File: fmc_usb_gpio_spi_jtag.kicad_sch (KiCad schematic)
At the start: 10 parts

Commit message: fmc_usb_gpio_spi_jtag.kicad_sch: update sheet pins
Signed-off-by: Huang Rui <vowstar@gmail.com>
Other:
- sheet FMC ports: added 12VP0, 3P3V, 3P3VAUX, GND, VADJ; removed none
- sheet GPIO ports: added GPIO[0..19]; removed none
- sheet JTAG ports: added JTAG{JTAG}; removed none
- sheet SDIO ports: added SDIO{SDIO}; removed none
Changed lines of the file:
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@@
       (effects (font (size 1.27 1.27)) (justify left top))
+    )
+    (pin "12VP0" output (at 260.35 50.8 270)
+      (effects (font (size 1.27 1.27)) (justify left))
+    )
+    (pin "3P3VAUX" output (at 257.81 50.8 270)
+      (effects (font (size 1.27 1.27)) (justify left))
+    )
+    (pin "GND" output (at 255.27 50.8 270)
+      (effects (font (size 1.27 1.27)) (justify left))
+    )
+    (pin "3P3V" output (at 252.73 50.8 270)
+      (effects (font (size 1.27 1.27)) (justify left))
+    )
+    (pin "VADJ" output (at 250.19 50.8 270)
+      (effects (font (size 1.27 1.27)) (justify left))
     )
     (instances
@@
       (effects (font (size 1.27 1.27)) (justify left top))
     )
-    (pin "USB_FS{USB_FS}" bidirectional (at 219.71 76.2 90)
+    (pin "USB_FS{USB_FS}" bidirectional (at 215.9 76.2 90)
       (effects (font (size 1.27 1.27)) (justify right))
     )
@@
       (effects (font (size 1.27 1.27)) (justify left top))
     )
+    (pin "JTAG{JTAG}" input (at 50.8 76.2 90)
+      (effects (font (size 1.27 1.27)) (justify right))
+    )
     (instances
       (project "fmc_usb_gpio_spi_jtag"
@@
     (property "Sheetfile" "gpio.kicad_sch" (at 137.16 107.2646 0)
       (effects (font (size 1.27 1.27)) (justify left top))
+    )
+    (pin "GPIO[0..19]" input (at 151.13 76.2 90)
+      (effects (font (size 1.27 1.27)) (justify right))
     )
     (instances
@@
       (effects (font (size 1.27 1.27)) (justify left top))
     )
+    (pin "SDIO{SDIO}" input (at 182.88 76.2 90)
+      (effects (font (size 1.27 1.27)) (justify right))
+    )
     (instances

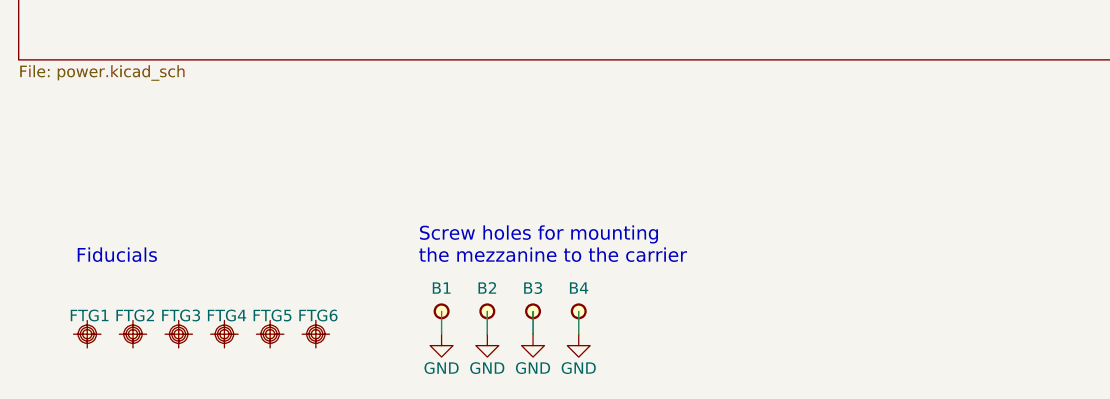
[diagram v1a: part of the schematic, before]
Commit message: fmc_usb_gpio_spi_jtag.kicad_sch: update fiducial and holes
Signed-off-by: Huang Rui <vowstar@gmail.com>
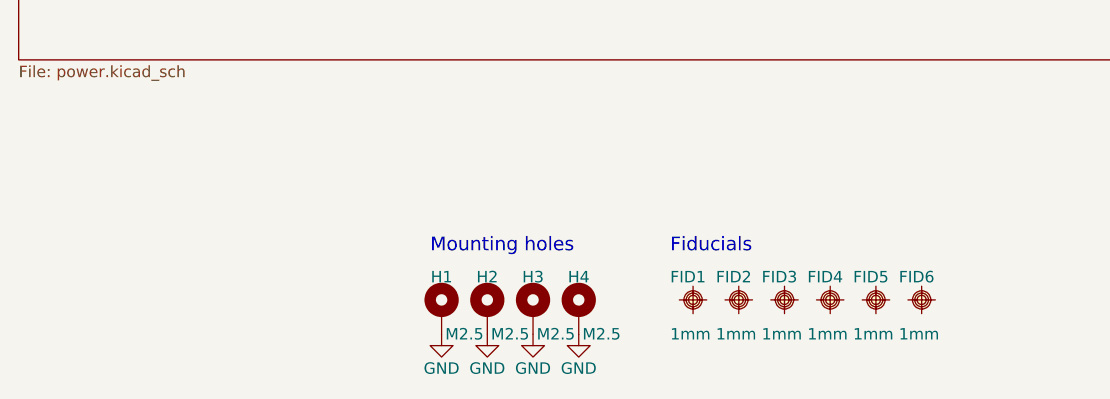
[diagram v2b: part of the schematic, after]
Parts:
- removed FTG1, FTG2, FTG3, FTG4, FTG5, FTG6: FIDUCIAL_TARGET_C100-200, Fiducial:Fiducial_1mm_Mask2mm, symbol Mechanical:Fiducial
- added FID1, FID2, FID3, FID4, FID5, FID6: 1mm, Fiducial:Fiducial_1mm_Mask2mm, symbol CHIPSAlliance_Mechanical:Fiducial
- H1: renamed from B1; value PLATED_HOLE2.7_PAD5.0 -> M2.5; symbol Mechanical:MountingHole_Pad -> CHIPSAlliance_Mechanical:MountingHole_Pad; Author CERN DEM JMW -> (none); Case (none) -> (none); Comment (none) -> (none); Component Kind Standard (No BOM) -> (none); Component Type Standard (No BOM) -> (none); ComponentHeight 0mm -> (none); ComponentLink1Description (none) -> (none); ComponentLink1URL (none) -> (none); ComponentLink2Description (none) -> (none); ComponentLink2URL (none) -> (none); CreateDate 09/27/11 00:00:00 -> (none); Database Table Name Pads -> (none); Family Plated Hole -> (none); Footprint Library Pads -> (none); Footprint Ref MTG270_500 -> (none); HelpURL Undefined -> (none); LatestRevisionDate 09/27/11 00:00:00 -> (none); Library Name .DbLib -> (none); Library Ref Single Terminal Socket -> (none); Manufacturer (none) -> (none); Manufacturer Part Number (none) -> (none); Manufacturer1 ComponentHeight (none) -> (none); Manufacturer1 Example (none) -> (none); Manufacturer1 Part Number (none) -> (none); Mounted No -> (none); PackageDescription Plated Through Hole: Hole Dia.=2.7mm Pad Dia.=5.0mm -> (none); Part Description Plated Through Hole: Hole Dia.=2.7mm Pad Dia.=5.0mm -> (none); Part Number PLATED_HOLE2.7_PAD5.0 -> (none); Pin Count 1 -> (none); SCEM (none) -> (none); SMD No -> (none); Sense No -> (none); Sense Comment (none) -> (none); Socket No -> (none); Status None -> (none); Status Comment (none) -> (none)
- H2: renamed from B2; value PLATED_HOLE2.7_PAD5.0 -> M2.5; symbol Mechanical:MountingHole_Pad -> CHIPSAlliance_Mechanical:MountingHole_Pad; Author CERN DEM JMW -> (none); Case (none) -> (none); Comment (none) -> (none); Component Kind Standard (No BOM) -> (none); Component Type Standard (No BOM) -> (none); ComponentHeight 0mm -> (none); ComponentLink1Description (none) -> (none); ComponentLink1URL (none) -> (none); ComponentLink2Description (none) -> (none); ComponentLink2URL (none) -> (none); CreateDate 09/27/11 00:00:00 -> (none); Database Table Name Pads -> (none); Family Plated Hole -> (none); Footprint Library Pads -> (none); Footprint Ref MTG270_500 -> (none); HelpURL Undefined -> (none); LatestRevisionDate 09/27/11 00:00:00 -> (none); Library Name .DbLib -> (none); Library Ref Single Terminal Socket -> (none); Manufacturer (none) -> (none); Manufacturer Part Number (none) -> (none); Manufacturer1 ComponentHeight (none) -> (none); Manufacturer1 Example (none) -> (none); Manufacturer1 Part Number (none) -> (none); Mounted No -> (none); PackageDescription Plated Through Hole: Hole Dia.=2.7mm Pad Dia.=5.0mm -> (none); Part Description Plated Through Hole: Hole Dia.=2.7mm Pad Dia.=5.0mm -> (none); Part Number PLATED_HOLE2.7_PAD5.0 -> (none); Pin Count 1 -> (none); SCEM (none) -> (none); SMD No -> (none); Sense No -> (none); Sense Comment (none) -> (none); Socket No -> (none); Status None -> (none); Status Comment (none) -> (none)
- H3: renamed from B3; value PLATED_HOLE2.7_PAD5.0 -> M2.5; symbol Mechanical:MountingHole_Pad -> CHIPSAlliance_Mechanical:MountingHole_Pad; Author CERN DEM JMW -> (none); Case (none) -> (none); Comment (none) -> (none); Component Kind Standard (No BOM) -> (none); Component Type Standard (No BOM) -> (none); ComponentHeight 0mm -> (none); ComponentLink1Description (none) -> (none); ComponentLink1URL (none) -> (none); ComponentLink2Description (none) -> (none); ComponentLink2URL (none) -> (none); CreateDate 09/27/11 00:00:00 -> (none); Database Table Name Pads -> (none); Family Plated Hole -> (none); Footprint Library Pads -> (none); Footprint Ref MTG270_500 -> (none); HelpURL Undefined -> (none); LatestRevisionDate 09/27/11 00:00:00 -> (none); Library Name .DbLib -> (none); Library Ref Single Terminal Socket -> (none); Manufacturer (none) -> (none); Manufacturer Part Number (none) -> (none); Manufacturer1 ComponentHeight (none) -> (none); Manufacturer1 Example (none) -> (none); Manufacturer1 Part Number (none) -> (none); Mounted No -> (none); PackageDescription Plated Through Hole: Hole Dia.=2.7mm Pad Dia.=5.0mm -> (none); Part Description Plated Through Hole: Hole Dia.=2.7mm Pad Dia.=5.0mm -> (none); Part Number PLATED_HOLE2.7_PAD5.0 -> (none); Pin Count 1 -> (none); SCEM (none) -> (none); SMD No -> (none); Sense No -> (none); Sense Comment (none) -> (none); Socket No -> (none); Status None -> (none); Status Comment (none) -> (none)
- H4: renamed from B4; value PLATED_HOLE2.7_PAD5.0 -> M2.5; symbol Mechanical:MountingHole_Pad -> CHIPSAlliance_Mechanical:MountingHole_Pad; Author CERN DEM JMW -> (none); Case (none) -> (none); Comment (none) -> (none); Component Kind Standard (No BOM) -> (none); Component Type Standard (No BOM) -> (none); ComponentHeight 0mm -> (none); ComponentLink1Description (none) -> (none); ComponentLink1URL (none) -> (none); ComponentLink2Description (none) -> (none); ComponentLink2URL (none) -> (none); CreateDate 09/27/11 00:00:00 -> (none); Database Table Name Pads -> (none); Family Plated Hole -> (none); Footprint Library Pads -> (none); Footprint Ref MTG270_500 -> (none); HelpURL Undefined -> (none); LatestRevisionDate 09/27/11 00:00:00 -> (none); Library Name .DbLib -> (none); Library Ref Single Terminal Socket -> (none); Manufacturer (none) -> (none); Manufacturer Part Number (none) -> (none); Manufacturer1 ComponentHeight (none) -> (none); Manufacturer1 Example (none) -> (none); Manufacturer1 Part Number (none) -> (none); Mounted No -> (none); PackageDescription Plated Through Hole: Hole Dia.=2.7mm Pad Dia.=5.0mm -> (none); Part Description Plated Through Hole: Hole Dia.=2.7mm Pad Dia.=5.0mm -> (none); Part Number PLATED_HOLE2.7_PAD5.0 -> (none); Pin Count 1 -> (none); SCEM (none) -> (none); SMD No -> (none); Sense No -> (none); Sense Comment (none) -> (none); Socket No -> (none); Status None -> (none); Status Comment (none) -> (none)
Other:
- note added: "Mounting holes"
- note removed: "Screw holes for mounting the mezzanine to the carrier"

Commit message: fmc_usb_gpio_spi_jtag.kicad_sch: change mounting holes
Signed-off-by: Huang Rui <vowstar@gmail.com>
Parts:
- H3, H4: footprint MountingHole:MountingHole_2.7mm_M2.5_Pad_Via -> MountingHole:MountingHole_2.7mm_M2.5_ISO14580_Pad
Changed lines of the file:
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@@
       (effects (font (size 1.27 1.27)))
     )
-    (property "Footprint" "MountingHole:MountingHole_2.7mm_M2.5_Pad_Via" (at 100.33 205.232 0)
+    (property "Footprint" "MountingHole:MountingHole_2.7mm_M2.5_ISO14580_Pad" (at 100.33 205.232 0)
       (effects (font (size 1.524 1.524)) (justify left) hide)
     )
@@
       (effects (font (size 1.27 1.27)))
     )
-    (property "Footprint" "MountingHole:MountingHole_2.7mm_M2.5_Pad_Via" (at 95.25 205.232 0)
-      (effects (font (size 1.524 1.524)) (justify left) hide)
-    )
+    (property "Footprint" "MountingHole:MountingHole_2.7mm_M2.5_ISO14580_Pad" (at 95.25 205.232 0)
+      (effects (font (size 1.524 1.524)) (justify left) hide)
+    )

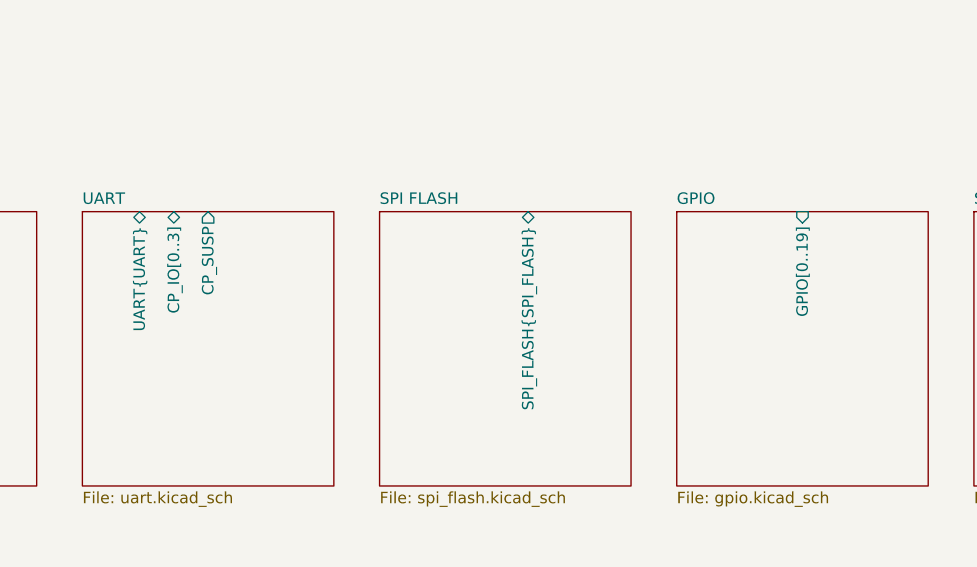
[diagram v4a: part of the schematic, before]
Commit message: *.kicad_sch: fix GPIO sheet pins
Signed-off-by: Huang Rui <vowstar@gmail.com>
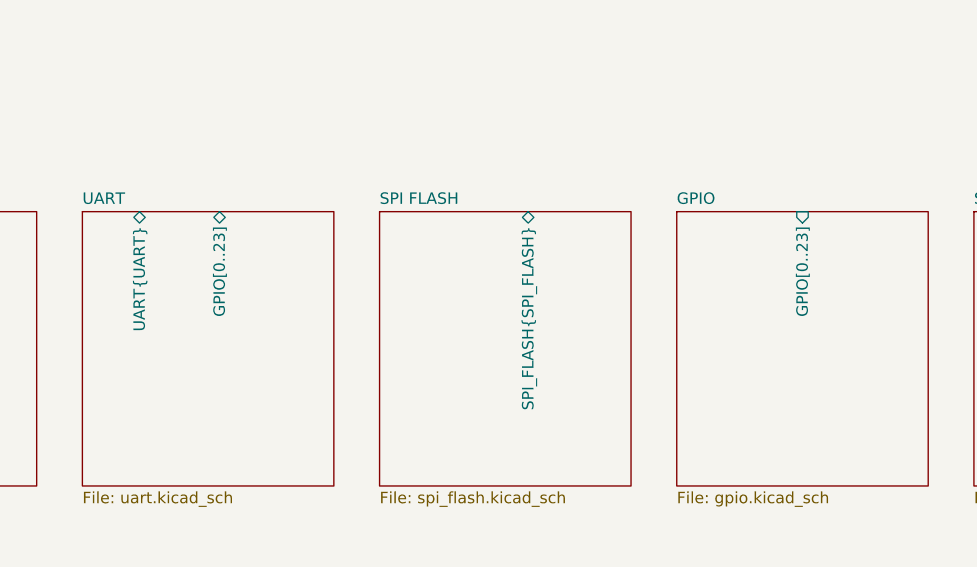
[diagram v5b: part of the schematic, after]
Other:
- sheet GPIO ports: added GPIO[0..23]; removed GPIO[0..19]
- sheet UART ports: added GPIO[0..23]; removed CP_IO[0..3], CP_SUSP
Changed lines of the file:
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@@
       (effects (font (size 1.27 1.27)) (justify right))
     )
-    (pin "CP_IO[0..3]" tri_state (at 81.28 76.2 90)
-      (effects (font (size 1.27 1.27)) (justify right))
-    )
-    (pin "CP_SUSP" output (at 85.09 76.2 90)
+    (pin "GPIO[0..23]" tri_state (at 86.36 76.2 90)
       (effects (font (size 1.27 1.27)) (justify right))
     )
@@
       (effects (font (size 1.27 1.27)) (justify left top))
     )
-    (pin "GPIO[0..19]" input (at 151.13 76.2 90)
+    (pin "GPIO[0..23]" input (at 151.13 76.2 90)
       (effects (font (size 1.27 1.27)) (justify right))
     )
